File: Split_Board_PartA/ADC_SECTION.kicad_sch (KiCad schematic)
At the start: 60 parts, among them J2 Conn_01x28, J2 Conn_01x37, J2 DC37_Receptacle, U26 MCP604, U27 MCP604, U28 ADC128S102CIMTX_NOPB

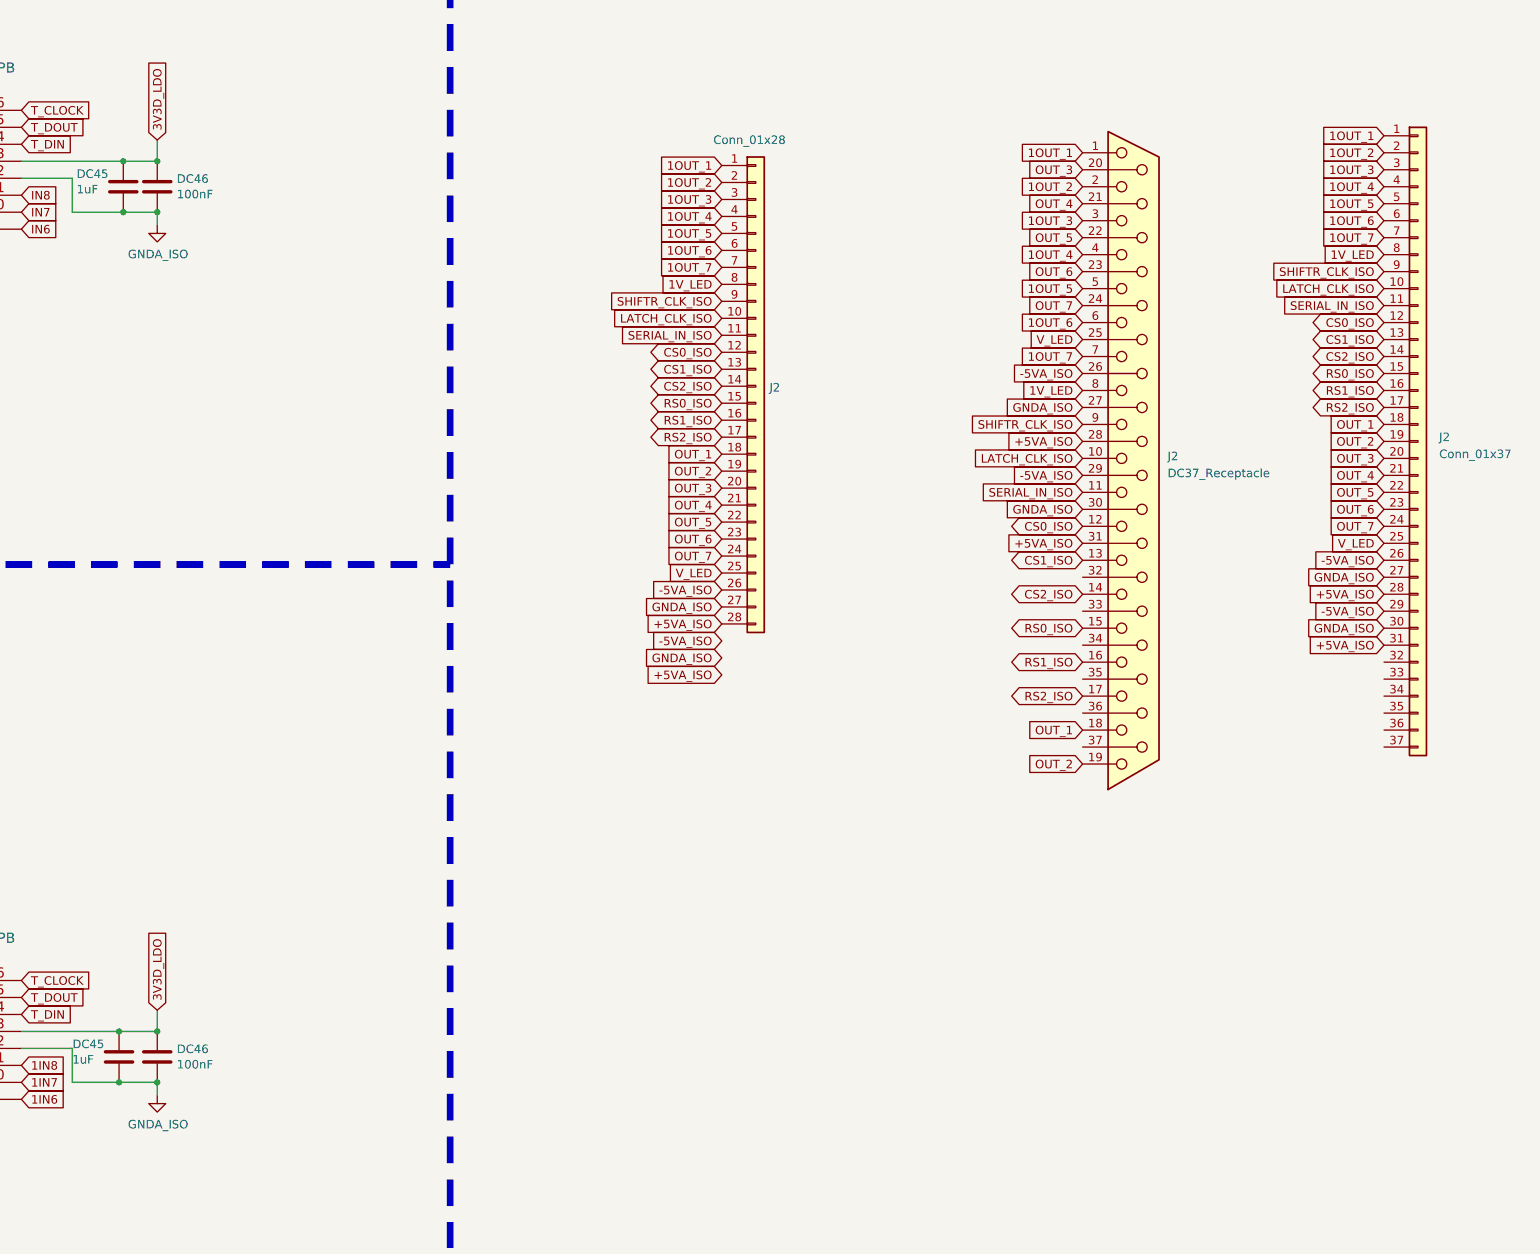
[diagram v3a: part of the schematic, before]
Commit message: changed the part A power section, added the ground GNDD_ISO
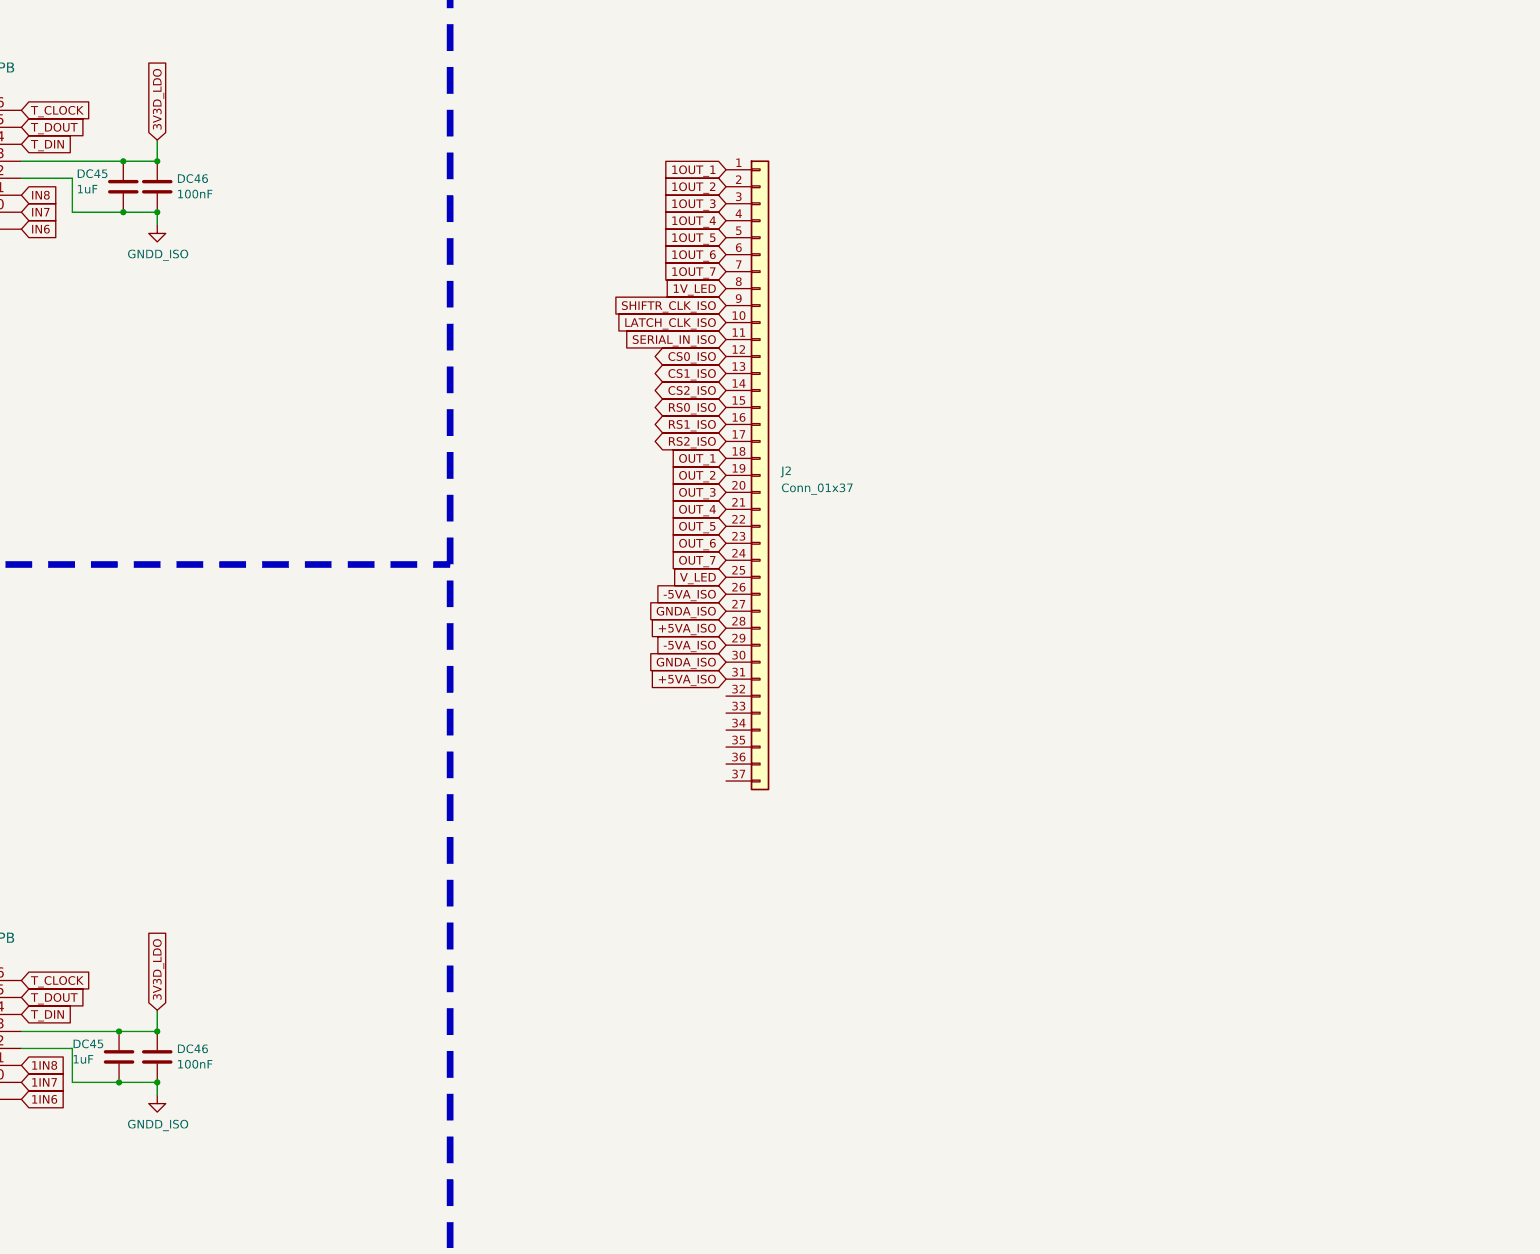
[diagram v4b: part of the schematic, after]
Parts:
- removed J2: Conn_01x28, SamacSys_Parts:522072833, symbol Connector_Generic:Conn_01x28
- removed J2: DC37_Receptacle, symbol Connector:DC37_Receptacle
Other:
- moved on the sheet: J2

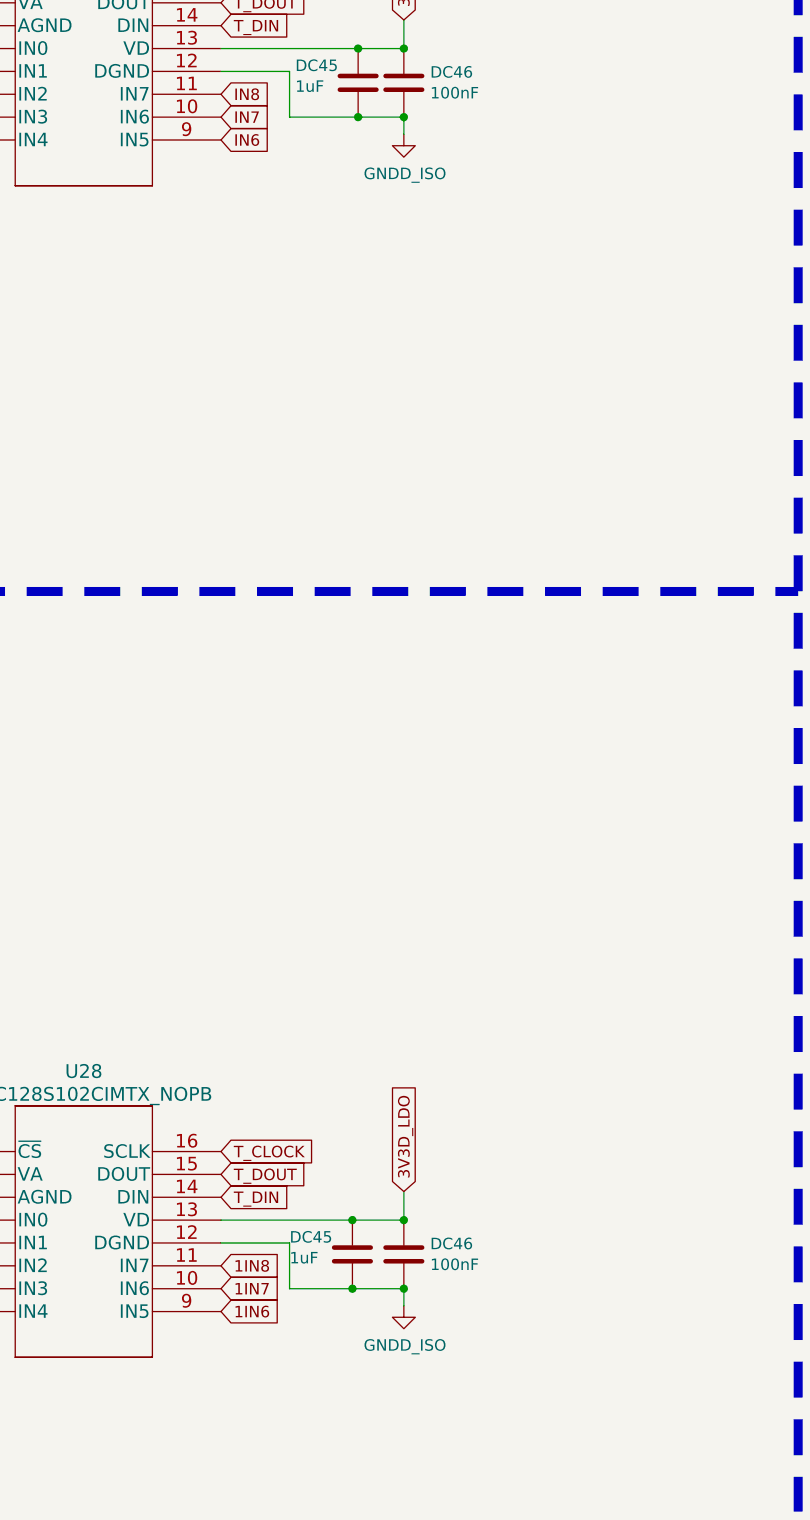
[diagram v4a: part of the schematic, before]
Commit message: eliminated the GNDD_ISO net
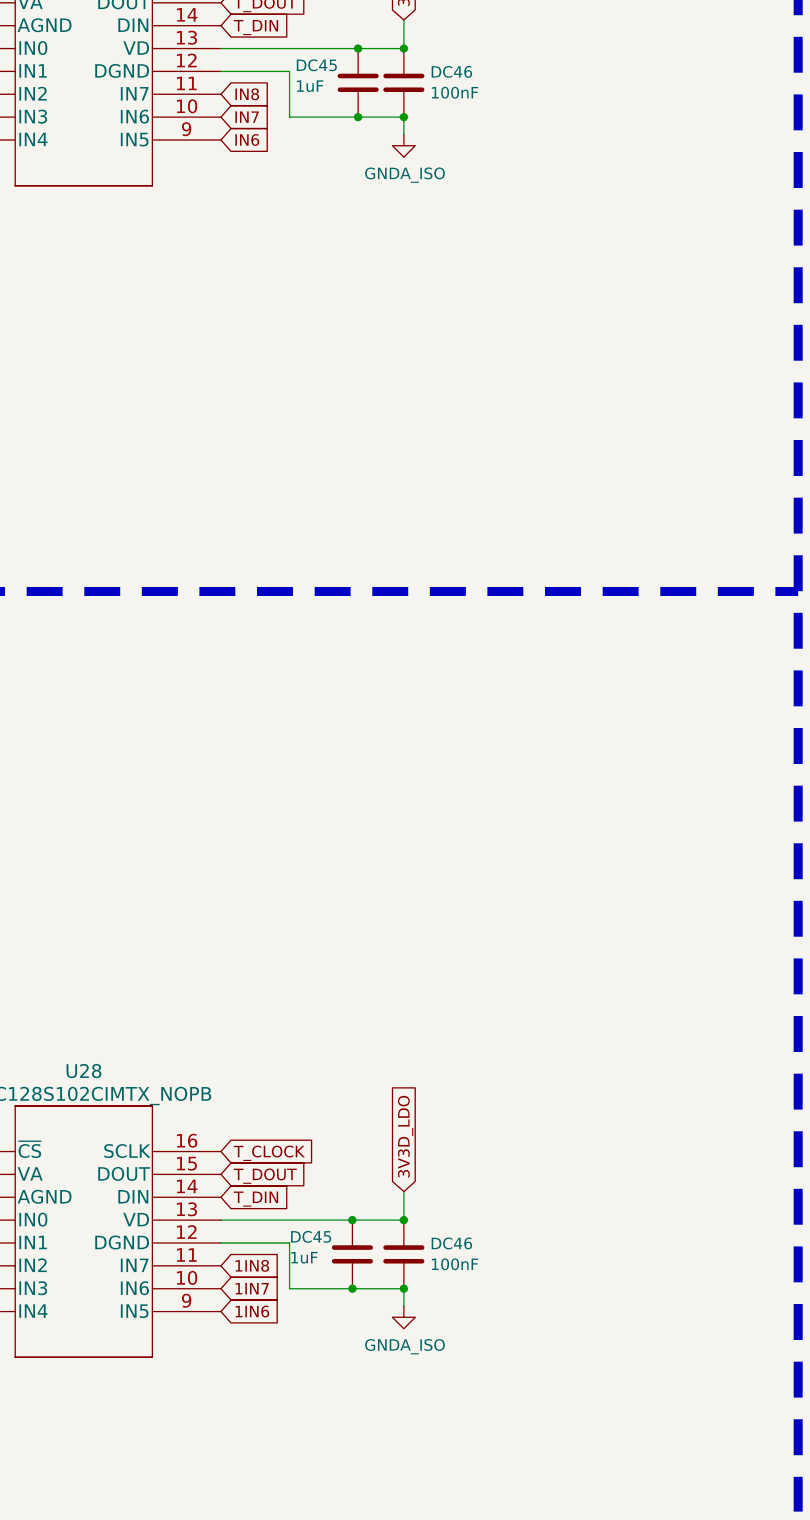
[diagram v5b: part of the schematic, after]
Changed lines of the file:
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@@
       (effects (font (size 1.27 1.27)) hide)
     )
-    (property "Value" "GNDD_ISO" (at 297.307 104.0892 0)
+    (property "Value" "GNDA_ISO" (at 297.307 104.0892 0)
       (effects (font (size 1.27 1.27)))
     )
@@
       (effects (font (size 1.27 1.27)) hide)
     )
-    (property "Value" "GNDD_ISO" (at 297.307 234.2642 0)
-      (effects (font (size 1.27 1.27)))
-    )
+    (property "Value" "GNDA_ISO" (at 297.307 234.2642 0)
+      (effects (font (size 1.27 1.27)))
+    )
